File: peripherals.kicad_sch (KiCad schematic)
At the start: 3 parts, among them U1 MIMX8MM6DVTLZAA

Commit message: ddr: add dual die support, misc work
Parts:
- added R100, R85, R86, R87, R88, R89, R90, R91, R92, R93, R94, R95, R96, R97, R98, R99: 10K, Resistor_SMD:R_0402_1005Metric, symbol Device:R
- added R113, R114: 4.7K, Resistor_SMD:R_0402_1005Metric, symbol Device:R
- gave numbers to parts that had none: 2
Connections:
- net VDD_1.8V: now also R100.1, R113.1, R114.1, R85.1, R86.1, R87.1, R88.1, R89.1, R90.1, R91.1, R92.1, R93.1, R94.1, R95.1, R96.1, R97.1, R98.1, R99.1
- net BT_CFG1: now reaches U1.AF15 (SAI1_RXD1)
- net BT_CFG1: now also R91.2
- net BT_CFG3: now reaches U1.AF17 (SAI1_RXD3)
- net BT_CFG3: now also R89.2
- net BT_CFG5: now reaches U1.AF18 (SAI1_RXD5)
- net BT_CFG5: now also R87.2
- net BT_CFG7: now reaches U1.AF19 (SAI1_RXD7)
- net BT_CFG7: now also R85.2
- net BT_CFG9: now reaches U1.AF20 (SAI1_TXD1)
- net BT_CFG9: now also R99.2
- net BT_CFG11: now reaches U1.AF21 (SAI1_TXD3)
- net BT_CFG11: now also R97.2
- net BT_CFG13: now reaches U1.AF22 (SAI1_TXD5)
- net BT_CFG13: now also R95.2
- net BT_CFG15: now reaches U1.AF23 (SAI1_TXD7)
- net BT_CFG15: now also R93.2
- net BT_CFG0: now reaches U1.AG15 (SAI1_RXD0)
- net BT_CFG0: now also R92.2
- net BT_CFG2: now reaches U1.AG17 (SAI1_RXD2)
- net BT_CFG2: now also R90.2
- net BT_CFG4: now reaches U1.AG18 (SAI1_RXD4)
- net BT_CFG4: now also R88.2
- net BT_CFG6: now reaches U1.AG19 (SAI1_RXD6)
- net BT_CFG6: now also R86.2
- net BT_CFG8: now reaches U1.AG20 (SAI1_TXD0)
- net BT_CFG8: now also R100.2
- net BT_CFG10: now reaches U1.AG21 (SAI1_TXD2)
- net BT_CFG10: now also R98.2
- net BT_CFG12: now reaches U1.AG22 (SAI1_TXD4)
- net BT_CFG12: now also R96.2
- net BT_CFG14: now reaches U1.AG23 (SAI1_TXD6)
- net BT_CFG14: now also R94.2
- net ~{PMIC_INT}: now reaches U1.AF13 (GPIO1_IO03)
- net SD2_VSELECT: now reaches U1.AG12 (GPIO1_IO04)
- net I2C1_SCL: now reaches U1.E9 (I2C1_SCL)
- net I2C1_SCL: now also R113.2
- net I2C1_SDA: now reaches U1.F9 (I2C1_SDA)
- net I2C1_SDA: now also R114.2
- no-connect marks 0 -> 66
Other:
- company: (none) -> Q-LAB
- title: (none) -> QSBC
- moved on the sheet: R78, R79, U1D, U1M, U1N, U1O, U1P

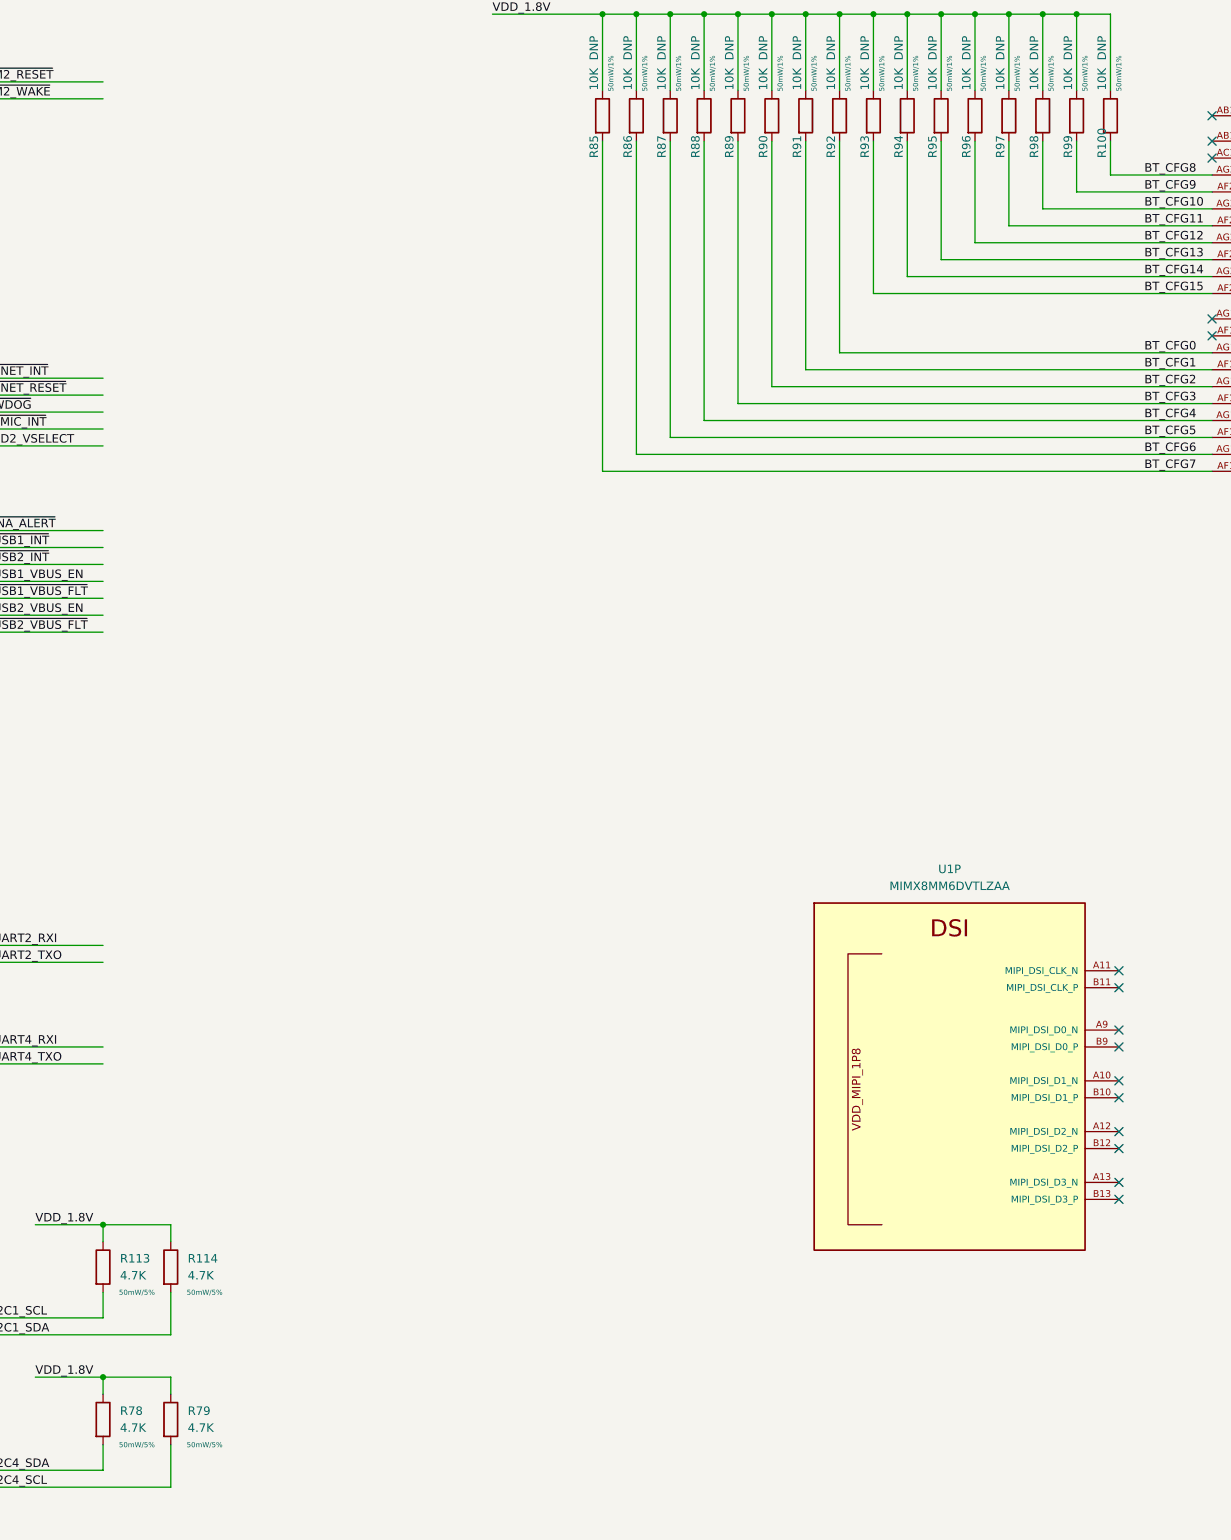
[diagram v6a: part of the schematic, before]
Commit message: fix ref desgigators, add table for dram config
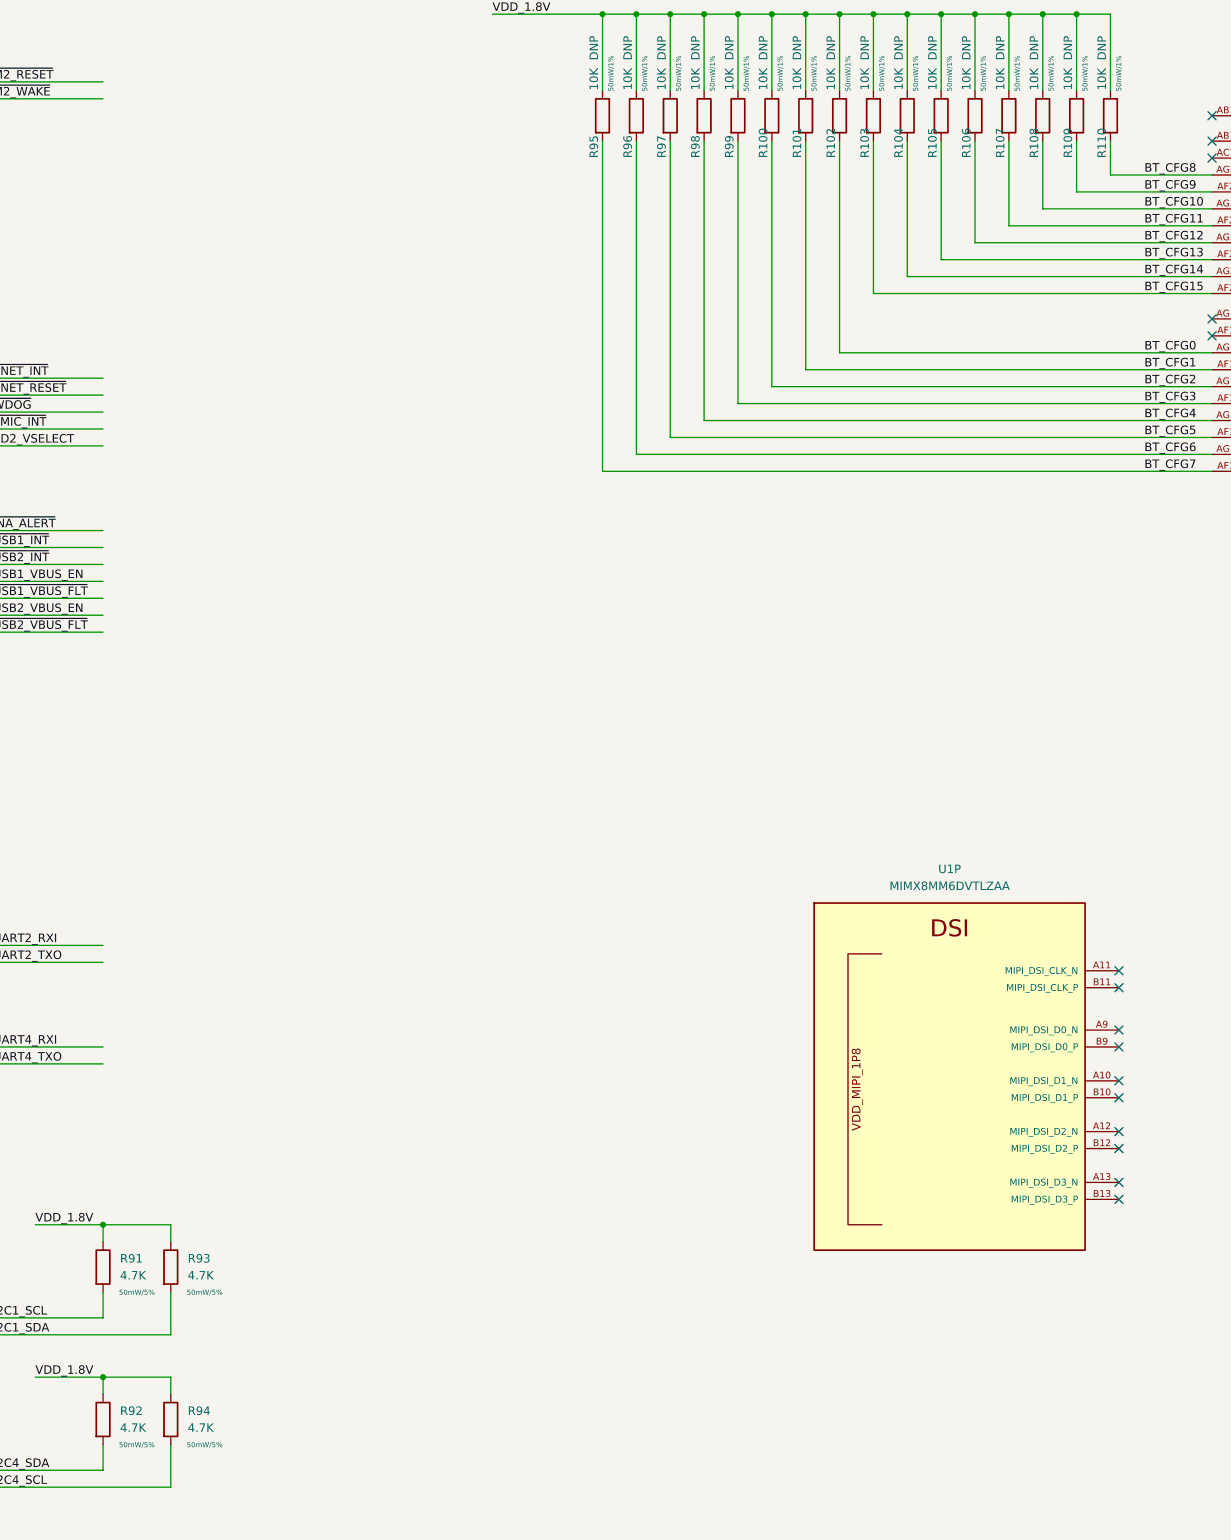
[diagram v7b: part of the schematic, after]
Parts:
- renumbered R90 to R100, R91 to R101, R92 to R102, R93 to R103, R94 to R104, R95 to R105, R96 to R106, R97 to R107, R98 to R108, R99 to R109, R100 to R110, R113 to R91, R78 to R92, R114 to R93, R79 to R94, R85 to R95, R86 to R96, R87 to R97, R88 to R98, R89 to R99
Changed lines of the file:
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@@
   (symbol (lib_id "Device:R") (at 280.67 54.61 0) (unit 1)
     (in_bom yes) (on_board yes)
-    (property "Reference" "R94" (id 0) (at 279.4 60.96 90)
+    (property "Reference" "R104" (id 0) (at 279.4 60.96 90)
       (effects (font (size 1.27 1.27)) (justify left))
     )
@@
   (symbol (lib_id "Device:R") (at 170.18 250.19 0) (unit 1)
     (in_bom yes) (on_board yes)
-    (property "Reference" "R79" (id 0) (at 172.72 248.9199 0)
+    (property "Reference" "R94" (id 0) (at 172.72 248.9199 0)
       (effects (font (size 1.27 1.27)) (justify left))
     )
@@
   (symbol (lib_id "Device:R") (at 250.19 54.61 0) (unit 1)
     (in_bom yes) (on_board yes)
-    (property "Reference" "R88" (id 0) (at 248.92 60.96 90)
+    (property "Reference" "R98" (id 0) (at 248.92 60.96 90)
       (effects (font (size 1.27 1.27)) (justify left))
     )
@@
   (symbol (lib_id "Device:R") (at 275.59 54.61 0) (unit 1)
     (in_bom yes) (on_board yes)
-    (property "Reference" "R93" (id 0) (at 274.32 60.96 90)
+    (property "Reference" "R103" (id 0) (at 274.32 60.96 90)
       (effects (font (size 1.27 1.27)) (justify left))
     )
@@
   (symbol (lib_id "Device:R") (at 270.51 54.61 0) (unit 1)
     (in_bom yes) (on_board yes)
-    (property "Reference" "R92" (id 0) (at 269.24 60.96 90)
+    (property "Reference" "R102" (id 0) (at 269.24 60.96 90)
       (effects (font (size 1.27 1.27)) (justify left))
     )
@@
   (symbol (lib_id "Device:R") (at 170.18 227.33 0) (unit 1)
     (in_bom yes) (on_board yes)
-    (property "Reference" "R114" (id 0) (at 172.72 226.0599 0)
+    (property "Reference" "R93" (id 0) (at 172.72 226.0599 0)
       (effects (font (size 1.27 1.27)) (justify left))
     )
@@
   (symbol (lib_id "Device:R") (at 265.43 54.61 0) (unit 1)
     (in_bom yes) (on_board yes)
-    (property "Reference" "R91" (id 0) (at 264.16 60.96 90)
+    (property "Reference" "R101" (id 0) (at 264.16 60.96 90)
       (effects (font (size 1.27 1.27)) (justify left))
     )
@@
   (symbol (lib_id "Device:R") (at 160.02 250.19 0) (unit 1)
     (in_bom yes) (on_board yes)
-    (property "Reference" "R78" (id 0) (at 162.56 248.9199 0)
+    (property "Reference" "R92" (id 0) (at 162.56 248.9199 0)
       (effects (font (size 1.27 1.27)) (justify left))
     )
@@
   (symbol (lib_id "Device:R") (at 245.11 54.61 0) (unit 1)
     (in_bom yes) (on_board yes)
-    (property "Reference" "R87" (id 0) (at 243.84 60.96 90)
+    (property "Reference" "R97" (id 0) (at 243.84 60.96 90)
       (effects (font (size 1.27 1.27)) (justify left))
     )
@@
   (symbol (lib_id "Device:R") (at 306.07 54.61 0) (unit 1)
     (in_bom yes) (on_board yes)
-    (property "Reference" "R99" (id 0) (at 304.8 60.96 90)
+    (property "Reference" "R109" (id 0) (at 304.8 60.96 90)
       (effects (font (size 1.27 1.27)) (justify left))
     )
@@
   (symbol (lib_id "Device:R") (at 295.91 54.61 0) (unit 1)
     (in_bom yes) (on_board yes)
-    (property "Reference" "R97" (id 0) (at 294.64 60.96 90)
+    (property "Reference" "R107" (id 0) (at 294.64 60.96 90)
       (effects (font (size 1.27 1.27)) (justify left))
     )
@@
   (symbol (lib_id "Device:R") (at 255.27 54.61 0) (unit 1)
     (in_bom yes) (on_board yes)
-    (property "Reference" "R89" (id 0) (at 254 60.96 90)
+    (property "Reference" "R99" (id 0) (at 254 60.96 90)
       (effects (font (size 1.27 1.27)) (justify left))
     )
@@
   (symbol (lib_id "Device:R") (at 300.99 54.61 0) (unit 1)
     (in_bom yes) (on_board yes)
-    (property "Reference" "R98" (id 0) (at 299.72 60.96 90)
+    (property "Reference" "R108" (id 0) (at 299.72 60.96 90)
       (effects (font (size 1.27 1.27)) (justify left))
     )
@@
   (symbol (lib_id "Device:R") (at 290.83 54.61 0) (unit 1)
     (in_bom yes) (on_board yes)
-    (property "Reference" "R96" (id 0) (at 289.56 60.96 90)
+    (property "Reference" "R106" (id 0) (at 289.56 60.96 90)
       (effects (font (size 1.27 1.27)) (justify left))
     )
@@
   (symbol (lib_id "Device:R") (at 285.75 54.61 0) (unit 1)
     (in_bom yes) (on_board yes)
-    (property "Reference" "R95" (id 0) (at 284.48 60.96 90)
+    (property "Reference" "R105" (id 0) (at 284.48 60.96 90)
       (effects (font (size 1.27 1.27)) (justify left))
     )
@@
   (symbol (lib_id "Device:R") (at 234.95 54.61 0) (unit 1)
     (in_bom yes) (on_board yes)
-    (property "Reference" "R85" (id 0) (at 233.68 60.96 90)
+    (property "Reference" "R95" (id 0) (at 233.68 60.96 90)
       (effects (font (size 1.27 1.27)) (justify left))
     )
@@
   (symbol (lib_id "Device:R") (at 240.03 54.61 0) (unit 1)
     (in_bom yes) (on_board yes)
-    (property "Reference" "R86" (id 0) (at 238.76 60.96 90)
+    (property "Reference" "R96" (id 0) (at 238.76 60.96 90)
       (effects (font (size 1.27 1.27)) (justify left))
     )
@@
   (symbol (lib_id "Device:R") (at 260.35 54.61 0) (unit 1)
     (in_bom yes) (on_board yes)
-    (property "Reference" "R90" (id 0) (at 259.08 60.96 90)
+    (property "Reference" "R100" (id 0) (at 259.08 60.96 90)
       (effects (font (size 1.27 1.27)) (justify left))
     )
@@
   (symbol (lib_id "Device:R") (at 160.02 227.33 0) (unit 1)
     (in_bom yes) (on_board yes)
-    (property "Reference" "R113" (id 0) (at 162.56 226.0599 0)
+    (property "Reference" "R91" (id 0) (at 162.56 226.0599 0)
       (effects (font (size 1.27 1.27)) (justify left))
     )
@@
   (symbol (lib_id "Device:R") (at 311.15 54.61 0) (unit 1)
     (in_bom yes) (on_board yes)
-    (property "Reference" "R100" (id 0) (at 309.88 60.96 90)
+    (property "Reference" "R110" (id 0) (at 309.88 60.96 90)
       (effects (font (size 1.27 1.27)) (justify left))
     )
